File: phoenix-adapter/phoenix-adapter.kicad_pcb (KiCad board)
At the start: 2 copper layers, 16.2 x 20 mm, 2 parts, among them CON101 RCJ-2223

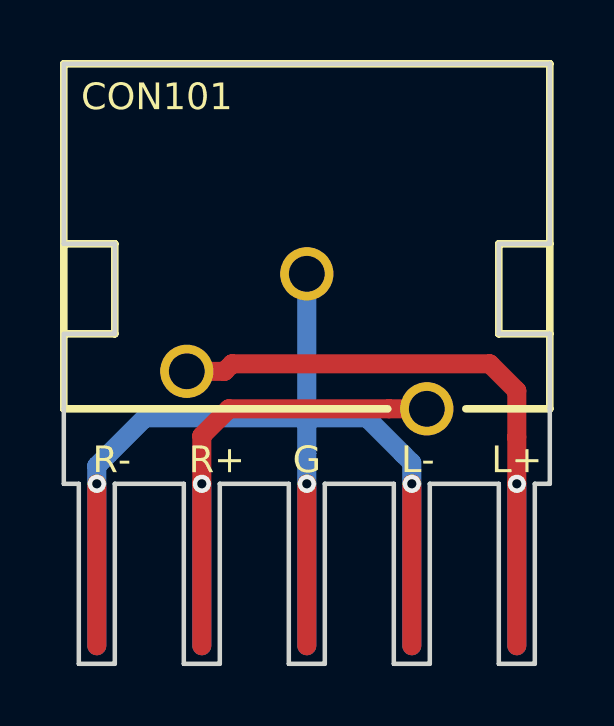
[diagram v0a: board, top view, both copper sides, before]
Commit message: First commit, replaced with JST XH connector
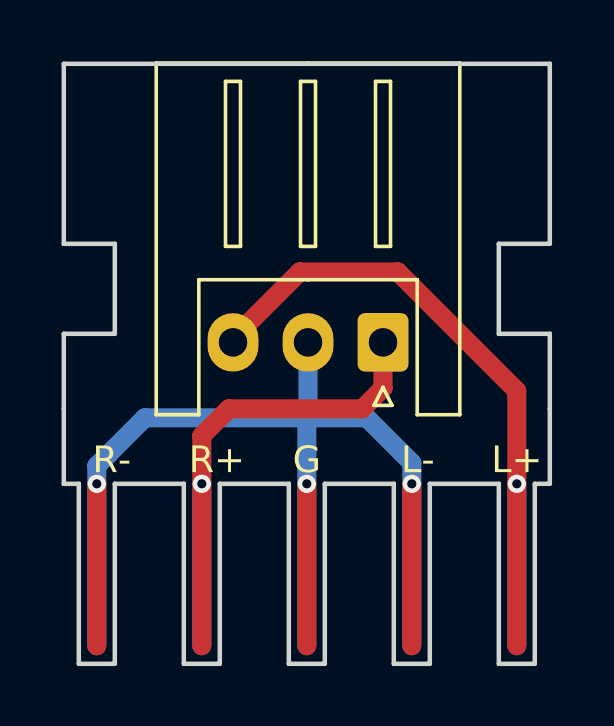
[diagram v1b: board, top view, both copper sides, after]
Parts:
- removed G***: LOGO, db-artwork:db-logo_7.5mm
- CON101: footprint db-thparts:RCJ-2223 -> Connector_JST:JST_XH_S03B-XH-A_1x03_P2.50mm_Horizontal
- moved CON101 9.63 mm to (142.2, 116.6), turned to 180 degrees
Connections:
- CON101 pad 1: GND -> /RIGHT
- CON101 pad 2: /LEFT -> GND
- CON101 pad 3: /RIGHT -> /LEFT
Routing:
- net GND: track 52.5 -> 50.2 mm
- net /LEFT: track 25.4 -> 26.0 mm

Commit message: Add back Rene's logo to the PCB, relabel some things on schematic
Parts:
- added G***: LOGO, db-artwork:db-logo_7.5mm, B.Cu at (143.5, 109.2)
- CON101: value RCJ-2223 -> JST-XH
